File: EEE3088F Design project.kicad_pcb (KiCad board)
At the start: 2 copper layers, 100 parts, among them J1 Conn_02x16_Odd_Even, J2 54-00285, J3 HUSB237, J4 Conn_01x02, Q1 NMOS, SW1 SW_SPDT, U1 Primary motors, U2 auxilliary motors, U3 TPS22950YBHR, U4 XL1509-3.3, U5 INA219AIDR, U6 TPS22950YBHR, U7 XL1509-5.0, U8 TP4056-42-ESOP8, U9 TPS61088RHLR

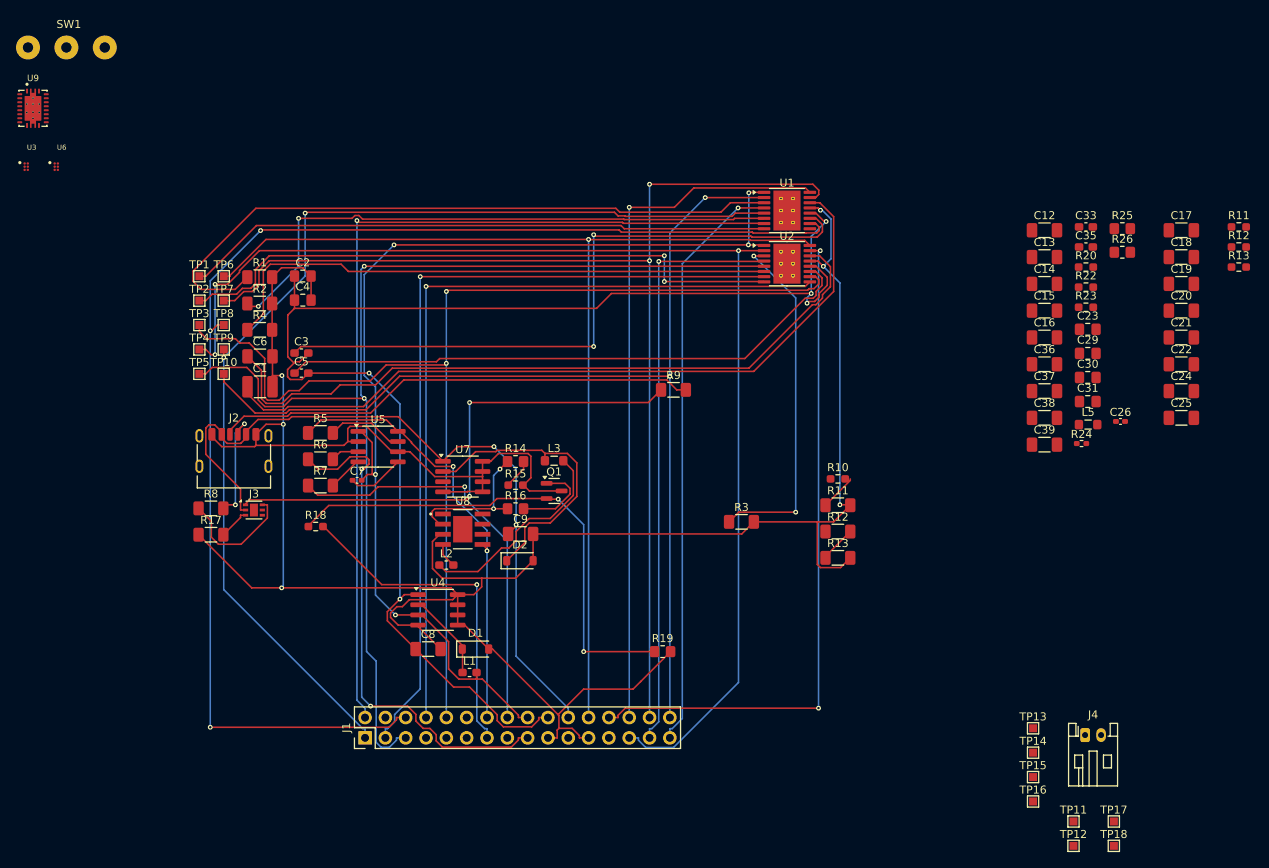
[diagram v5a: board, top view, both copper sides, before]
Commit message: Removed old backups and updated KiCad files
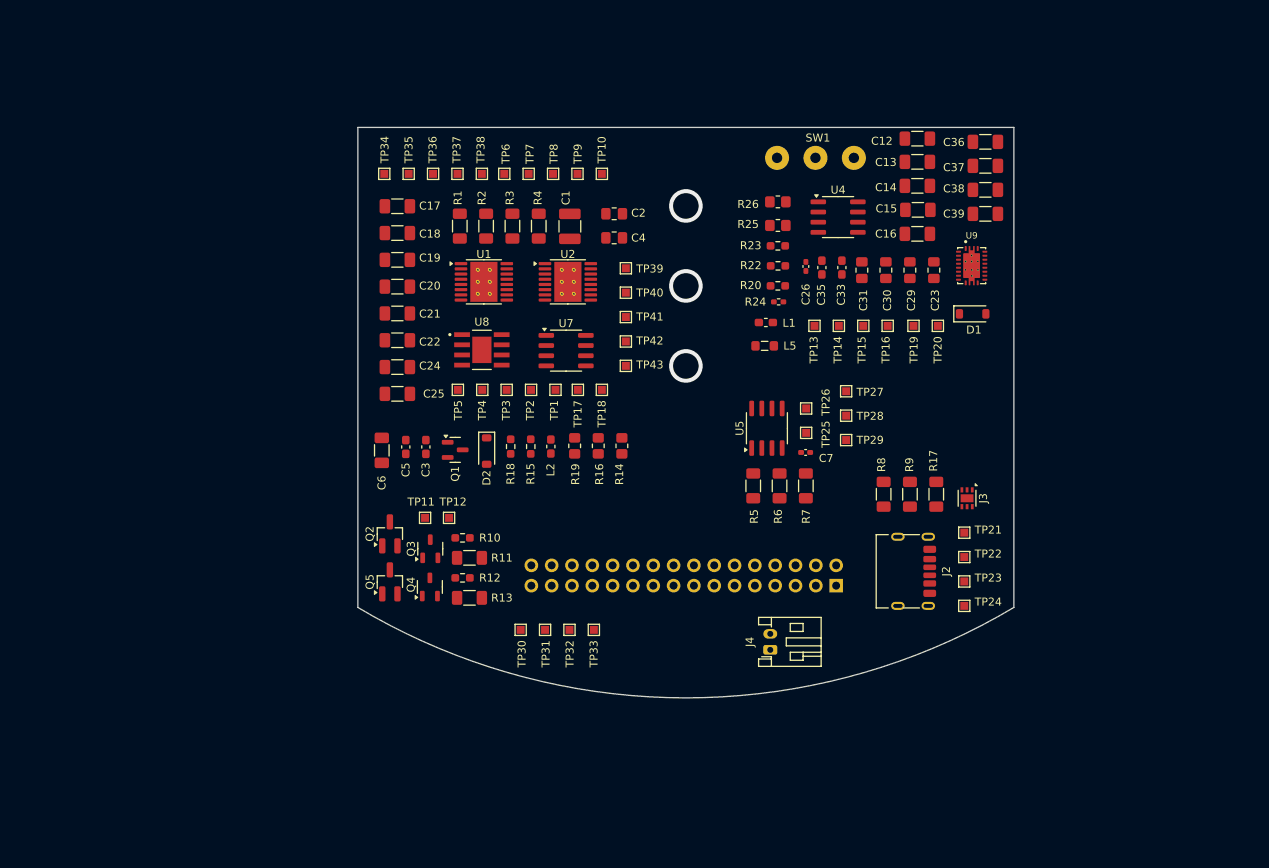
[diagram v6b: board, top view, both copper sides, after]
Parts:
- removed C8, C9: 1uF, Capacitor_SMD:C_1206_3216Metric_Pad1.33x1.80mm_HandSolder
- removed L3: 47uH, Inductor_SMD:L_0805_2012Metric_Pad1.05x1.20mm_HandSolder
- removed the R11 at (169.0, 105.9)
- removed the R11 at (219.1, 71.1)
- removed the R12 at (219.1, 73.6)
- removed the R12 at (169.0, 109.2)
- removed the R13 at (219.1, 76.2)
- removed the R13 at (169.0, 112.5)
- removed U3, U6: TPS22950YBHR, TPS22950YBHR:IC_TPS22950YBHR
- added Q2: PMOS, Package_TO_SOT_SMD:SOT-23_Handsoldering, F.Cu at (113.0, 109.5)
- added Q3: AO3400A, Package_TO_SOT_SMD:SOT-23-3, F.Cu at (118.0, 111.4)
- added Q4: AO3400A, Package_TO_SOT_SMD:SOT-23-3, F.Cu at (118.0, 116.1)
- added Q5: PMOS, Package_TO_SOT_SMD:SOT-23_Handsoldering, F.Cu at (113.0, 115.5)
- added R11: 1M, Resistor_SMD:R_1206_3216Metric_Pad1.30x1.75mm_HandSolder, F.Cu at (123.0, 112.5)
- added R12: 220, Resistor_SMD:R_0603_1608Metric_Pad0.98x0.95mm_HandSolder, F.Cu at (122.1, 115.0)
- added R13: 1M, Resistor_SMD:R_1206_3216Metric_Pad1.30x1.75mm_HandSolder, F.Cu at (123.0, 117.5)
- added TP19: TestPoint, TestPoint:TestPoint_Pad_1.0x1.0mm, F.Cu at (178.4, 83.5)
- added TP20: TestPoint, TestPoint:TestPoint_Pad_1.0x1.0mm, F.Cu at (181.5, 83.5)
- added TP21: TestPoint, TestPoint:TestPoint_Pad_1.0x1.0mm, F.Cu at (184.8, 109.3)
- added TP22: TestPoint, TestPoint:TestPoint_Pad_1.0x1.0mm, F.Cu at (184.8, 112.4)
- added TP23: TestPoint, TestPoint:TestPoint_Pad_1.0x1.0mm, F.Cu at (184.8, 115.5)
- added TP24: TestPoint, TestPoint:TestPoint_Pad_1.0x1.0mm, F.Cu at (184.8, 118.5)
- added TP25: TestPoint, TestPoint:TestPoint_Pad_1.0x1.0mm, F.Cu at (165.0, 96.9)
- added TP26: TestPoint, TestPoint:TestPoint_Pad_1.0x1.0mm, F.Cu at (165.0, 93.8)
- added TP27: TestPoint, TestPoint:TestPoint_Pad_1.0x1.0mm, F.Cu at (170.0, 91.7)
- added TP28: TestPoint, TestPoint:TestPoint_Pad_1.0x1.0mm, F.Cu at (170.0, 94.7)
- added TP29: TestPoint, TestPoint:TestPoint_Pad_1.0x1.0mm, F.Cu at (170.0, 97.8)
- added TP30: TestPoint, TestPoint:TestPoint_Pad_1.0x1.0mm, F.Cu at (129.3, 121.5)
- added TP31: TestPoint, TestPoint:TestPoint_Pad_1.0x1.0mm, F.Cu at (132.4, 121.5)
- added TP32: TestPoint, TestPoint:TestPoint_Pad_1.0x1.0mm, F.Cu at (135.4, 121.5)
- added TP33: TestPoint, TestPoint:TestPoint_Pad_1.0x1.0mm, F.Cu at (138.5, 121.5)
- added TP34: TestPoint, TestPoint:TestPoint_Pad_1.0x1.0mm, F.Cu at (112.3, 64.5)
- added TP35: TestPoint, TestPoint:TestPoint_Pad_1.0x1.0mm, F.Cu at (115.3, 64.5)
- added TP36: TestPoint, TestPoint:TestPoint_Pad_1.0x1.0mm, F.Cu at (118.4, 64.5)
- added TP37: TestPoint, TestPoint:TestPoint_Pad_1.0x1.0mm, F.Cu at (121.5, 64.5)
- added TP38: TestPoint, TestPoint:TestPoint_Pad_1.0x1.0mm, F.Cu at (124.5, 64.5)
- added TP39: TestPoint, TestPoint:TestPoint_Pad_1.0x1.0mm, F.Cu at (142.5, 76.3)
- added TP40: TestPoint, TestPoint:TestPoint_Pad_1.0x1.0mm, F.Cu at (142.5, 79.3)
- added TP41: TestPoint, TestPoint:TestPoint_Pad_1.0x1.0mm, F.Cu at (142.5, 82.4)
- added TP42: TestPoint, TestPoint:TestPoint_Pad_1.0x1.0mm, F.Cu at (142.5, 85.5)
- added TP43: TestPoint, TestPoint:TestPoint_Pad_1.0x1.0mm, F.Cu at (142.5, 88.5)
- J1: moved to B.Cu
- R10: value 2.2k -> 220
- moved U9 119.0 mm to (185.7, 76.0)
- moved C17 98.0 mm to (113.9, 68.5)
- moved C18 98.0 mm to (113.9, 71.9)
- moved C19 98.0 mm to (113.9, 75.2)
- moved C20 98.0 mm to (113.9, 78.6)
- moved C21 98.0 mm to (113.9, 82.0)
- moved C22 98.0 mm to (113.9, 85.3)
- moved C24 98.0 mm to (113.9, 88.7)
- moved C25 98.0 mm to (113.9, 92.0)
- moved SW1 94.6 mm to (166.2, 62.5)
- moved R17 90.8 mm to (181.3, 104.5), turned to 90 degrees
- moved TP11 89.5 mm to (117.4, 107.5)
- moved J3 89.2 mm to (185.2, 105.0), turned to -90 degrees
- moved TP12 88.2 mm to (120.4, 107.5)
- moved TP17 86.0 mm to (136.5, 91.5), turned to -90 degrees
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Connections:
- J2 pad S1: (no net) -> GND
- J3 pad 7: (no net) -> GND
- R10 pad 1: Net-(U3-ILIM) -> CTRL_EXT_LOAD1
- R10 pad 2: GND -> Net-(Q3-G)
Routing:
- net GND: track 342.6 -> 0.00 mm, vias 6 -> 3
- net 5V_Out: track 175.4 -> 0.00 mm, vias 5 -> 0
- net MOTOR2_CTRL2: track 163.7 -> 0.00 mm, vias 3 -> 0
- net MOTOR3_A_OUT: track 153.2 -> 0.00 mm, vias 3 -> 0
- net MOTOR1_CTRL2: track 146.2 -> 0.00 mm, vias 2 -> 0
- net MOTOR4_CTRL2: track 142.0 -> 0.00 mm, vias 2 -> 0
- net MOTOR4_B_OUT: track 140.0 -> 0.00 mm, vias 2 -> 0
- net 3V3_Out: track 137.3 -> 0.00 mm, vias 5 -> 0
- net MOTOR2_B_OUT: track 136.1 -> 0.00 mm, vias 2 -> 0
- net MOTOR3_CTRL1: track 135.3 -> 0.00 mm, vias 1 -> 0
- net MOTOR1_A_OUT: track 134.5 -> 0.00 mm, vias 2 -> 0
- net MOTOR2_A_OUT: track 113.6 -> 0.00 mm, vias 1 -> 0
- net MOTOR4_A_OUT: track 102.6 -> 0.00 mm, vias 1 -> 0
- net MOTOR4_CTRL1: track 102.1 -> 0.00 mm, vias 1 -> 0
- net HV: track 94.5 -> 0.00 mm, vias 2 -> 0
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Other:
- board outline added: 82 x 71.3 mm

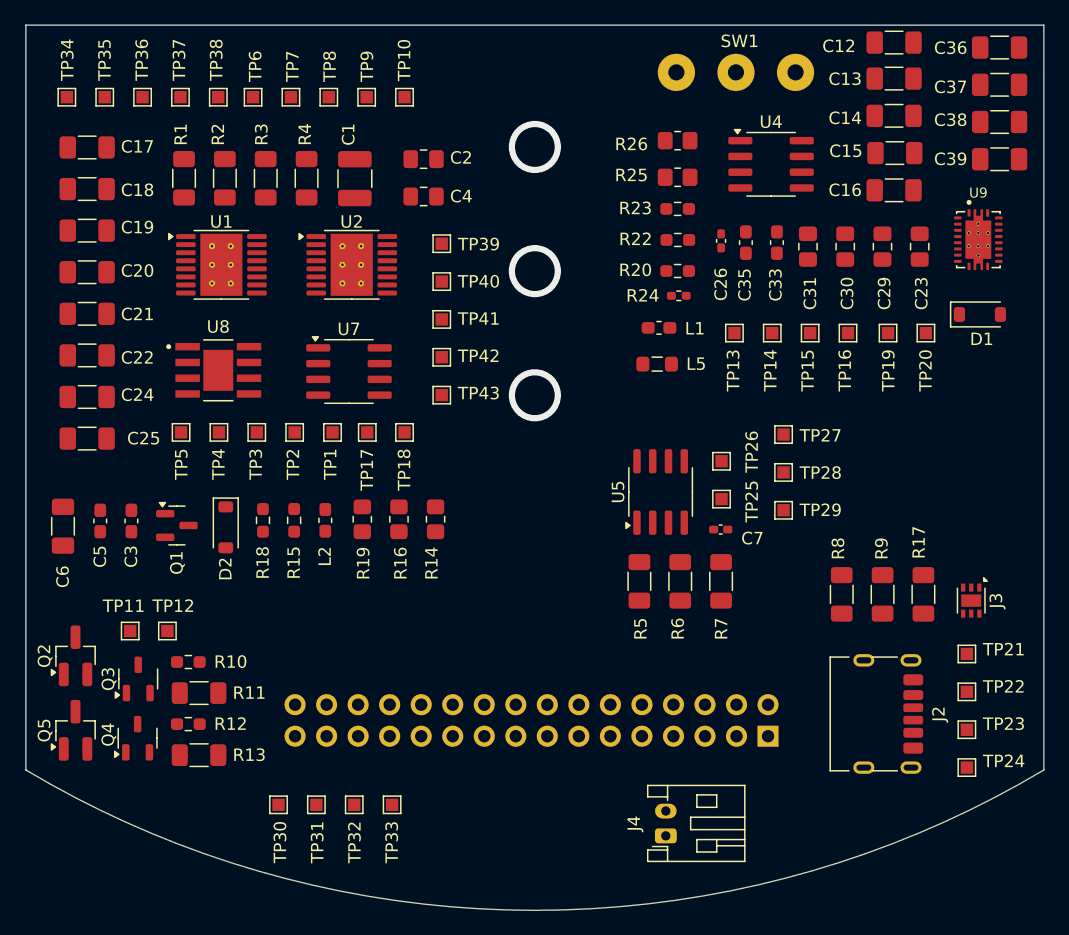
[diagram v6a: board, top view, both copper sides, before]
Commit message: Removed old backups and updated KiCad files
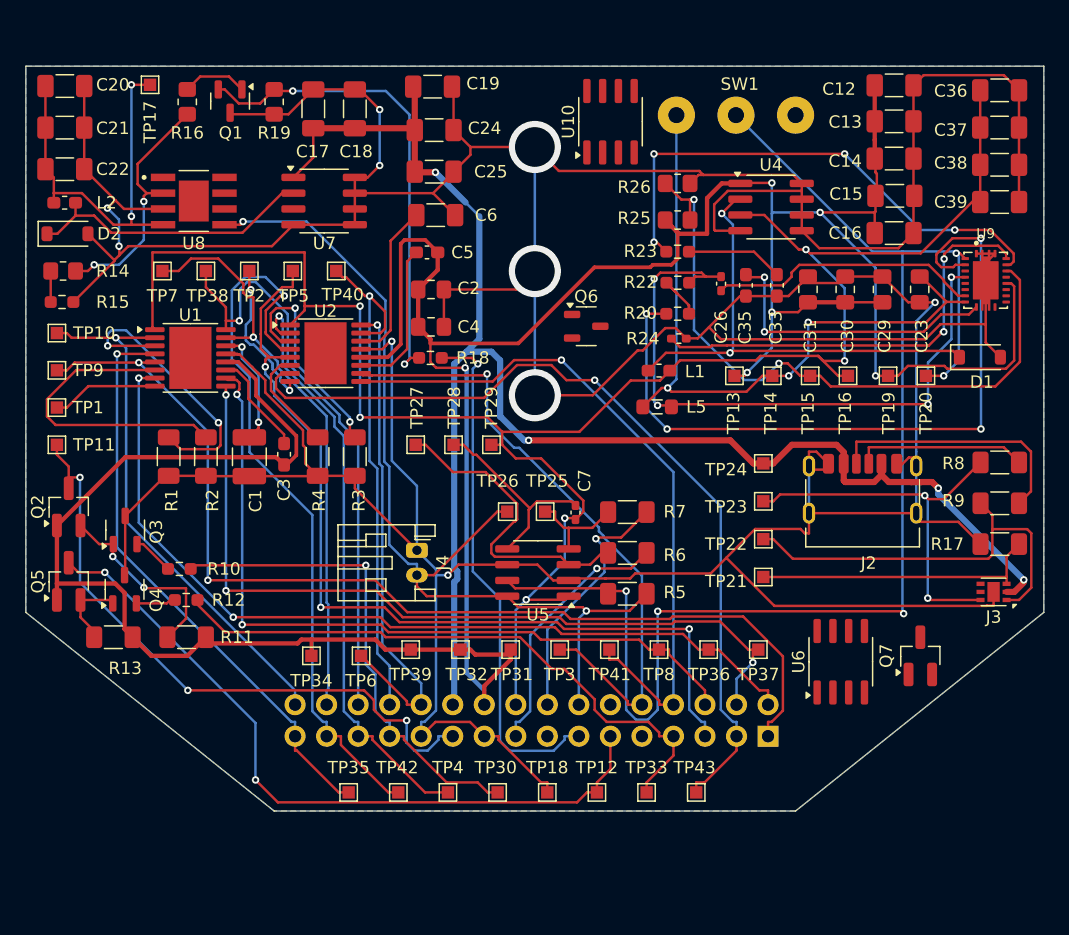
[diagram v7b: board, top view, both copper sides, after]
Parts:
- added Q6: AO3400A, Package_TO_SOT_SMD:SOT-23-3, F.Cu at (154.1, 83.0)
- added Q7: PMOS, Package_TO_SOT_SMD:SOT-23_Handsoldering, F.Cu at (181.1, 109.5)
- added U10: INA219AIDR, Package_SO:SOIC-8_3.9x4.9mm_P1.27mm, F.Cu at (156.1, 66.5)
- added U6: INA219AIDR, Package_SO:SOIC-8_3.9x4.9mm_P1.27mm, F.Cu at (174.6, 110.0)
- U1, U2: footprint Package_SO:HTSSOP-16-1EP_4.4x5mm_P0.65mm_EP3.4x5mm_Mask2.46x2.31mm_ThermalVias -> Package_SO:HTSSOP-16-1EP_4.4x5mm_P0.65mm_EP3.4x5mm_Mask2.46x2.31mm
- U9: footprint TPS61088RHLR:IC_TPS61088RHLR -> TPS61088RHLR:TPS61088RHLR
- moved TP37 64.4 mm to (168.0, 109.0), turned to 0 degrees
- moved TP36 63.7 mm to (164.0, 109.0), turned to -90 degrees
- moved TP35 59.3 mm to (135.0, 120.5)
- moved TP8 51.8 mm to (160.0, 109.0), turned to -90 degrees
- moved TP34 49.1 mm to (132.0, 109.5), turned to -90 degrees
- moved TP6 45.8 mm to (136.0, 109.5), turned to -90 degrees
- moved C6 39.1 mm to (142.0, 74.0), turned to 0 degrees
- moved TP43 38.0 mm to (163.0, 120.5), turned to 90 degrees
- moved R16 37.7 mm to (122.0, 64.9), turned to 90 degrees
- moved TP12 37.0 mm to (155.0, 120.5)
- moved R14 36.1 mm to (112.0, 78.5), turned to 180 degrees
- moved C24 35.3 mm to (141.9, 67.2)
- moved C25 35.3 mm to (141.9, 70.5)
- moved TP42 35.2 mm to (139.0, 120.5), turned to 90 degrees
- moved Q1 34.5 mm to (125.5, 64.8), turned to -90 degrees
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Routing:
- net GND: track 0.00 -> 481.9 mm, vias 3 -> 10
- net 5V_Out: track 0.00 -> 263.5 mm, vias 0 -> 6
- net 3V3_Out: track 0.00 -> 158.8 mm, vias 0 -> 6
- net HV: track 0.00 -> 128.2 mm, vias 0 -> 4
- net VCC: track 0.00 -> 115.1 mm, vias 0 -> 5
- net MOTOR2_B_OUT: track 0.00 -> 84.9 mm, vias 0 -> 2
- net Battery: track 0.00 -> 77.4 mm, vias 0 -> 2
- net MOTOR4_B_OUT: track 0.00 -> 71.9 mm, vias 0 -> 3
- net MOTOR2_A_OUT: track 0.00 -> 70.4 mm, vias 0 -> 2
- net MOTOR4_A_OUT: track 0.00 -> 69.5 mm, vias 0 -> 1
- net MOTOR2_CTRL1: track 0.00 -> 66.6 mm, vias 0 -> 3
- net MOTOR2_CTRL2: track 0.00 -> 61.9 mm, vias 0 -> 2
- net Net-(U9-FSW): track 0.00 -> 59.5 mm, vias 0 -> 4
- net MOTOR3_B_OUT: track 0.00 -> 58.9 mm, vias 0 -> 1
- net EXT_LOAD2_OUT: track 0.00 -> 58.5 mm, vias 0 -> 2
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- added copper zone on B.Cu, net GND
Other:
- board size 82 x 71.3 mm -> 82 x 60 mm
- board text added: "Hannah Owen & Phila Hanyama OWNHAN001 & HNYPHI001 Group number: 25"
- board text added: "Warning: Contains traces of genius."

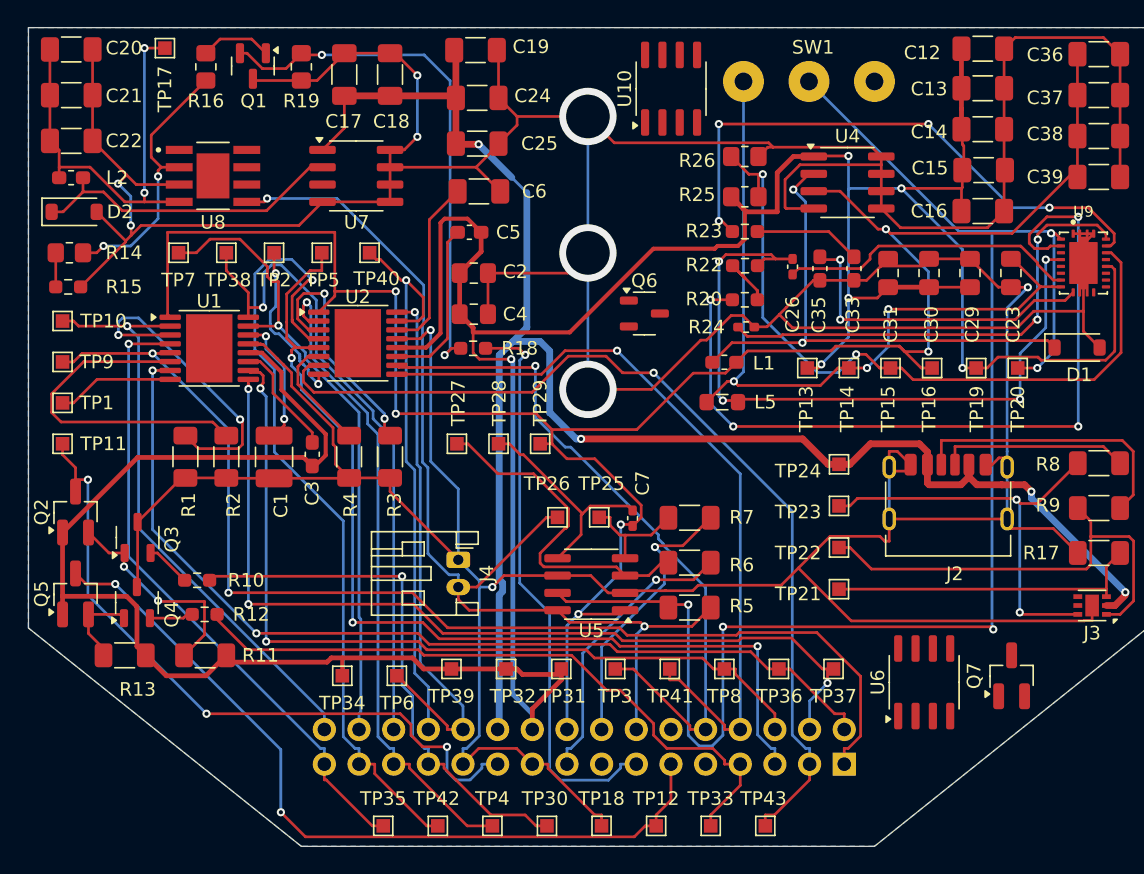
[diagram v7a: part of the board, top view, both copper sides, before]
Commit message: Removed old backups and updated KiCad files
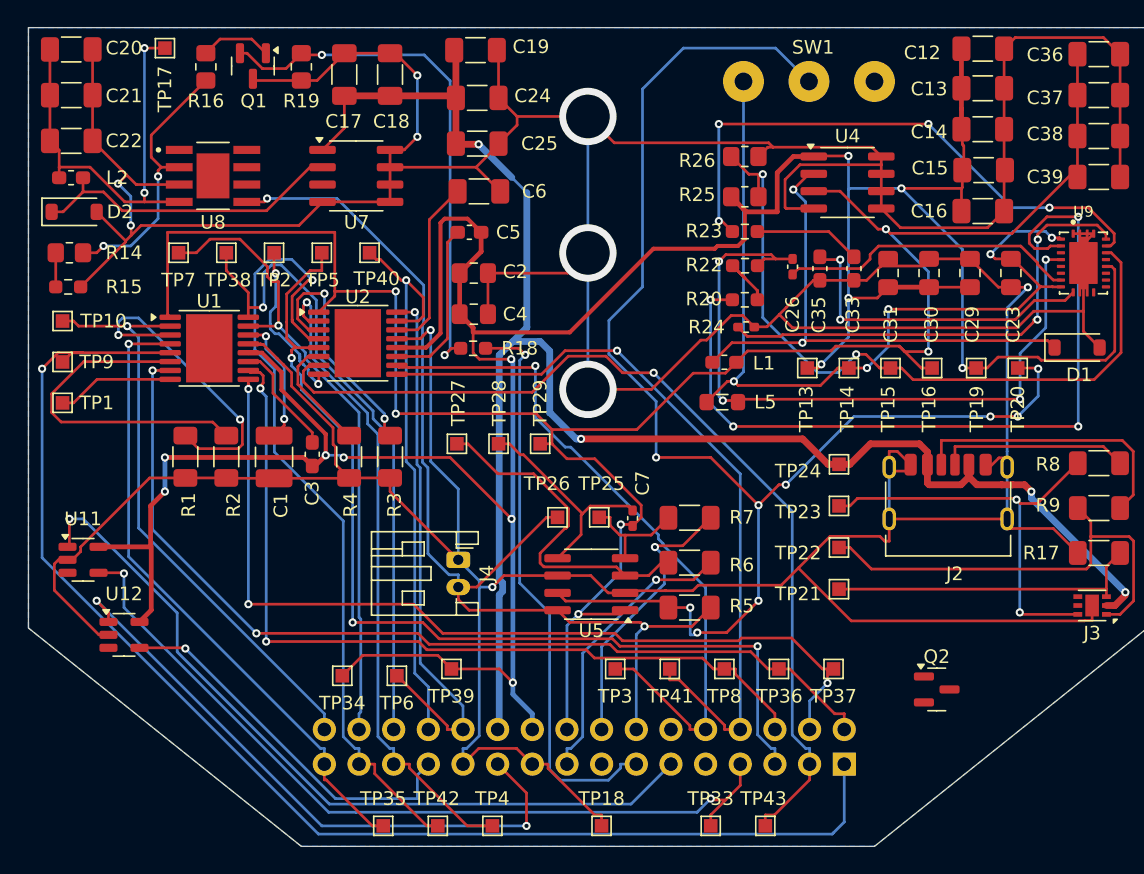
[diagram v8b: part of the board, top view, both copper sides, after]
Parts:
- removed Q3, Q4, Q6: AO3400A, Package_TO_SOT_SMD:SOT-23-3
- removed Q5, Q7: PMOS, Package_TO_SOT_SMD:SOT-23_Handsoldering
- removed R10, R12: 220, Resistor_SMD:R_0603_1608Metric_Pad0.98x0.95mm_HandSolder
- removed R11, R13: 1M, Resistor_SMD:R_1206_3216Metric_Pad1.30x1.75mm_HandSolder
- removed TP11, TP12, TP30, TP31, TP32: TestPoint, TestPoint:TestPoint_Pad_1.0x1.0mm
- removed U10, U6: INA219AIDR, Package_SO:SOIC-8_3.9x4.9mm_P1.27mm
- added U11: RT9742CGJ5, Package_TO_SOT_SMD:TSOT-23-5, F.Cu at (113.0, 101.0)
- added U12: RT9742CGJ5, Package_TO_SOT_SMD:TSOT-23-5, F.Cu at (116.0, 106.5)
- Q2: value PMOS -> NMOS; footprint Package_TO_SOT_SMD:SOT-23_Handsoldering -> Package_TO_SOT_SMD:SOT-23
- moved Q2 64.4 mm to (175.6, 110.5), turned to 0 degrees
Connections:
- net /3V3 5V output/FB renamed /3V3 and 5V output/FB
- net /battery/5V renamed Vcharge
- net Net-(U8-PROG) renamed Vprog
- C23 pad 1: Net-(SW1-A) -> Vswitch
- L5 pad 1: Net-(SW1-A) -> Vswitch
- Q2 pad 1: 5V_Out -> unconnected-(Q2-D-Pad1)
- Q2 pad 2: Net-(Q2-G) -> unconnected-(Q2-G-Pad2)
- Q2 pad 3: EXT_LOAD1_OUT -> unconnected-(Q2-S-Pad3)
- SW1 pad 1: Net-(SW1-A) -> Vswitch
- TP14 pad 1: Net-(SW1-A) -> Vswitch
- U9 pad 2: VCC -> Vswitch
- U9 pad 9: Net-(SW1-A) -> Vswitch
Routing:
- net Vswitch: track 0.00 -> 64.3 mm, vias 0 -> 5
- net Net-(SW1-A): track 56.6 -> 0.00 mm, vias 3 -> 0
- net 5V_Out: track 263.5 -> 245.2 mm, vias 6 -> 12
- net Net-(Q2-G): track 15.8 -> 0.00 mm, vias 2 -> 0
- net MOTOR2_B_OUT: track 84.9 -> 97.3 mm, vias 2 -> 1
- net CTRL_EXT_LOAD1: track 39.7 -> 27.8 mm
- net CTRL_EXT_LOAD2: track 49.4 -> 60.6 mm, vias 0 -> 2
- net GND: track 481.9 -> 492.0 mm
- net VCC: track 115.1 -> 105.4 mm, vias 5 -> 9
- net Net-(Q4-D): track 6.17 -> 0.00 mm
- net EXT_LOAD1_OUT: track 51.1 -> 45.6 mm, vias 3 -> 2
- net Net-(Q3-G): track 3.33 -> 0.00 mm
- net Net-(Q4-G): track 2.84 -> 0.00 mm
- net EXT_LOAD2_OUT: track 58.5 -> 57.7 mm, vias 2 -> 1
